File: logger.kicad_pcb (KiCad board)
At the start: 2 copper layers, 30 x 30 mm, 62 parts, among them J1 USB_C_Receptacle_USB2.0_16P, J2 Conn_01x02_Pin, SW1 BOOT0, U1 STM32U535CBTx, U10 LM66100DCK, U2 USBLC6-2SC6, U3 TPS7A0533PDBZ, U4 LM66100DCK, U5 W25Q128JVP, U6 BMP581, U7 MMC5983MA, U8 ADXL375, U9 LSM6DSV16X, Y1 32.768KHz

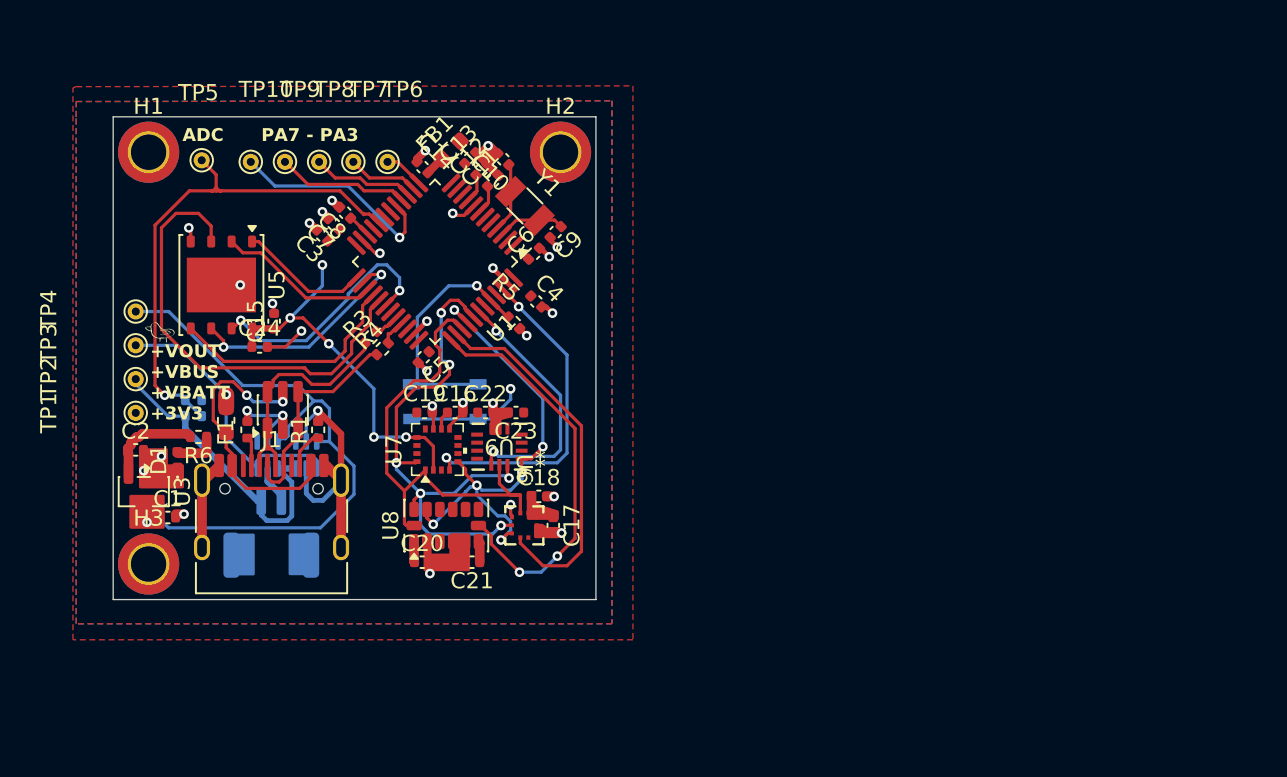
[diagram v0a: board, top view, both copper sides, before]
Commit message: schematic update
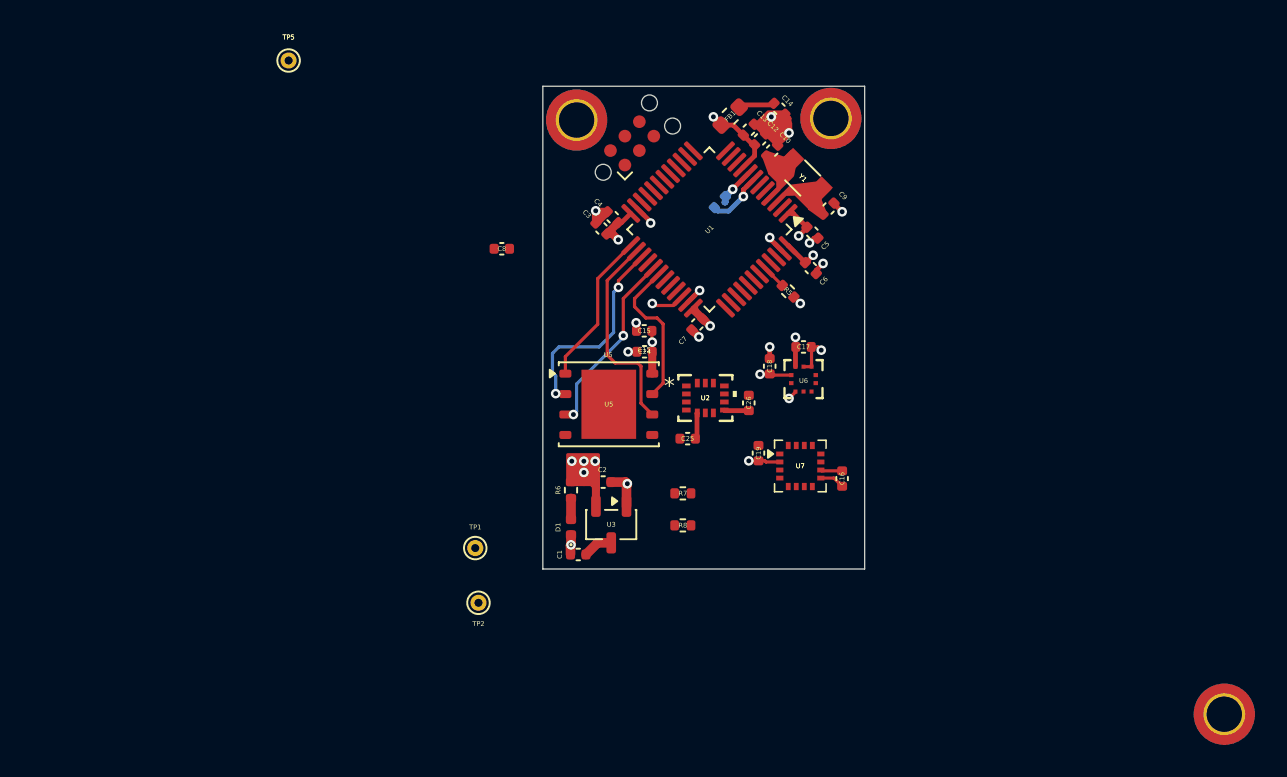
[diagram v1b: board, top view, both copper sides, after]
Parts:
- removed C20: 1uF, Capacitor_SMD:C_0402_1005Metric
- removed C21, C22, C23: 100nF, Capacitor_SMD:C_0402_1005Metric
- removed F1: Polyfuse_Small, Fuse:Fuse_0603_1608Metric
- removed J2: Conn_01x02_Pin, Connector_JST:JST_GH_BM02B-GHS-TBT_1x02-1MP_P1.25mm_Vertical
- removed R1, R2: 5.1kR, Resistor_SMD:R_0402_1005Metric
- removed R3, R4: 22R, Resistor_SMD:R_0402_1005Metric
- removed SW1: BOOT0, Button_Switch_SMD:SW_Push_1P1T_NO_Vertical_Wuerth_434133025816
- removed TP10: PA7, TestPoint:TestPoint_THTPad_D1.0mm_Drill0.5mm
- removed TP3: VBUS, TestPoint:TestPoint_THTPad_D1.0mm_Drill0.5mm
- removed TP4: VOUT, TestPoint:TestPoint_THTPad_D1.0mm_Drill0.5mm
- removed TP6: PA3, TestPoint:TestPoint_THTPad_D1.0mm_Drill0.5mm
- removed TP7: PA4, TestPoint:TestPoint_THTPad_D1.0mm_Drill0.5mm
- removed TP8: PA5, TestPoint:TestPoint_THTPad_D1.0mm_Drill0.5mm
- removed TP9: PA6, TestPoint:TestPoint_THTPad_D1.0mm_Drill0.5mm
- removed U10, U4: LM66100DCK, Package_TO_SOT_SMD:SOT-363_SC-70-6
- removed U8: ADXL375, Package_LGA:LGA-14_3x5mm_P0.8mm_LayoutBorder1x6y
- removed U9: LSM6DSV16X, LSM6DSV16X:LGA-14L_STM-L
- added C25: 100nF, Capacitor_SMD:C_0402_1005Metric, F.Cu at (92.0, 125.5)
- added C26: 100nF, Capacitor_SMD:C_0402_1005Metric, F.Cu at (95.8, 123.3)
- C11: moved to B.Cu
- J1: value USB_C_Receptacle_USB2.0_16P -> TC2030; footprint Connector_USB:USB_C_Receptacle_HRO_TYPE-C-31-M-12 -> Connector:Tag-Connect_TC2030-IDC-NL_2x03_P1.27mm_Vertical
- R6: value 100R -> 300R
- R7, R8: moved to F.Cu
- U2: value USBLC6-2SC6 -> ISM6HG256X; footprint Package_TO_SOT_SMD:SOT-23-6 -> ISM6HG256XTR:LGA14L_2P5X3_STM
- moved H2 54.0 mm to (125.3, 142.6)
- moved H3 50.6 mm to (100.9, 105.6)
- moved J1 32.9 mm to (88.5, 107.1), turned to 45 degrees
- moved R8 31.4 mm to (91.7, 130.9), turned to 0 degrees
- moved R7 30.8 mm to (91.7, 128.9), turned to 0 degrees
- moved U3 29.1 mm to (87.2, 130.8)
- moved C2 29.1 mm to (86.7, 128.2)
- moved H1 26.7 mm to (85.1, 105.7)
- moved U2 26.3 mm to (93.1, 123.0), turned to 0 degrees
- moved C1 25.6 mm to (85.2, 132.7), turned to 180 degrees
- moved TP2 25.4 mm to (79.0, 135.7), turned to 0 degrees
- moved C5 25.4 mm to (99.8, 112.7), turned to -45 degrees
- moved U5 25.2 mm to (87.1, 123.4), turned to 0 degrees
- moved D1 24.8 mm to (84.7, 131.0)
- moved C16 24.4 mm to (101.6, 128.0), turned to -90 degrees
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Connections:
- C1 pad 1: VOUT -> VBATT
- C11 pad 1: Net-(U1-NRST) -> /~{RESET}
- U1 pad 13: /PA3 -> unconnected-(U1-PA3-Pad13)
- U1 pad 14: /PA4 -> unconnected-(U1-PA4-Pad14)
- U1 pad 15: /PA5 -> /SPI1_SCK
- U1 pad 16: /PA6 -> unconnected-(U1-PA6-Pad16)
- U1 pad 17: /PA7 -> unconnected-(U1-PA7-Pad17)
- U1 pad 32: /USB_DN -> unconnected-(U1-PA11-Pad32)
- U1 pad 33: /USB_DP -> unconnected-(U1-PA12-Pad33)
- U1 pad 34: unconnected-(U1-PA13-Pad34) -> /DEBUG_SWDIO
- U1 pad 37: /SPI_ACCEL -> /DEBUG_SWCLK
- U1 pad 38: /SPI_BARO -> unconnected-(U1-PA15-Pad38)
- U1 pad 39: /SPI1_SCK -> /DEBUG_SWO
- U1 pad 42: /SPI_IMU -> unconnected-(U1-PB6-Pad42)
- U1 pad 43: unconnected-(U1-PB7-Pad43) -> /SPI_IMU
- U1 pad 45: unconnected-(U1-PB8-Pad45) -> /SPI_BARO
- U1 pad 7: Net-(U1-NRST) -> /~{RESET}
- U2 pad 1: /D- -> /SPI1_MISO
- U2 pad 3: /D+ -> GND
- U2 pad 4: /D+ -> unconnected-(U2-INT1-Pad4)
- U2 pad 5: Net-(U2-VBUS) -> +3V3
- U2 pad 6: /D- -> GND
- U3 pad 3: VOUT -> VBATT
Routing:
- net VOUT: track 38.7 -> 0.00 mm, vias 1 -> 0
- net /SPI1_MOSI: track 34.8 -> 0.00 mm, vias 6 -> 0
- net GND: track 62.7 -> 29.6 mm, vias 31 -> 19
- net /ADC1_IN17: track 32.3 -> 0.00 mm, vias 1 -> 0
- net /SPI1_MISO: track 30.5 -> 0.00 mm, vias 6 -> 0
- net /SPI1_SCK: track 29.9 -> 0.00 mm
- net /SPI_ACCEL: track 25.2 -> 0.00 mm, vias 2 -> 0
- net /SPI_BARO: track 23.0 -> 0.00 mm
- net /SPI_MAG: track 20.6 -> 0.00 mm, vias 2 -> 0
- net VBUS: track 18.2 -> 0.00 mm, vias 1 -> 0
- net Net-(U2-VBUS): track 17.7 -> 0.00 mm, vias 2 -> 0
- net VBATT: track 19.0 -> 1.87 mm
- net /FLASH_WP: track 28.6 -> 11.6 mm, vias 0 -> 2
- net /SPI_IMU: track 16.0 -> 0.00 mm, vias 2 -> 0
- net /D-: track 15.0 -> 0.00 mm
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- added copper zone on In2.Cu, net +3V3
- added copper zone on In1.Cu, net GND
- removed copper zone on F.Cu, net +3V3
- removed copper zone on B.Cu, net GND
- removed copper zone on F.Cu, net GND
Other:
- board size 30 x 30 mm -> 20 x 30 mm
- copper layers 2 -> 4
- board text removed: "+VOUT +VBUS +VBATT +3V3"
- board text removed: "ADC"
- board text removed: "Aozora - v0.${REVISION}"
- board text removed: "PA7 - PA3"
